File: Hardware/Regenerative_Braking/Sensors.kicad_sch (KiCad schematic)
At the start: 0 parts

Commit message: edited till inverter circuit
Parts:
- added ACS712-30A1, ACS712-30A2, ACS712-30A3: (no value), Regen_braking:ACS712_Module_27x12mm, symbol Regen_braking:ACS712-30A
- added ACS712-30A4, ACS712-30A5, ACS712-30A6: (no value), Regen_braking:Solderpad_acs712_INOUT, symbol Regen_braking:solder_pad_acs712_inout
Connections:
- new net 5V: ACS712-30A1. (VCC), ACS712-30A2. (VCC), ACS712-30A3. (VCC)
- new net GND: ACS712-30A1. (VCC), ACS712-30A2. (VCC), ACS712-30A3. (VCC), ACS712-30A4. (OUT), ACS712-30A5. (OUT), ACS712-30A6. (OUT)
- new net Iin1: ACS712-30A4. (OUT)
- new net Iin2: ACS712-30A5. (OUT)
- new net Iin3: ACS712-30A6. (OUT)
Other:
- note added: "INVERTER SIDE CURRENT SENSING"

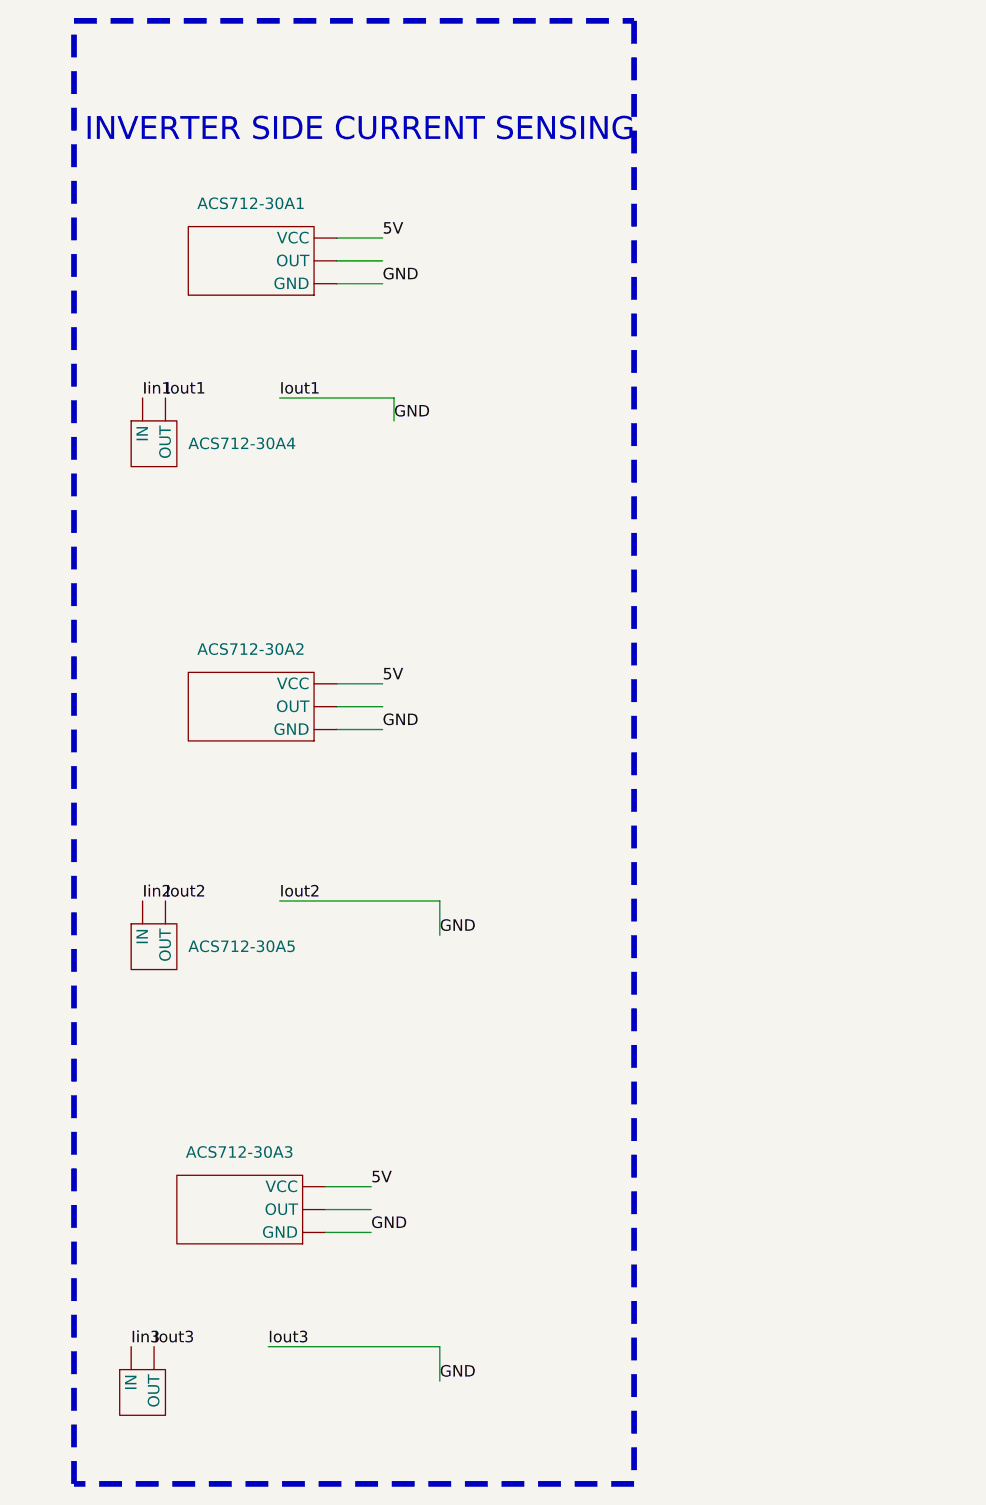
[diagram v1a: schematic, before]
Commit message: started with sensing circuits
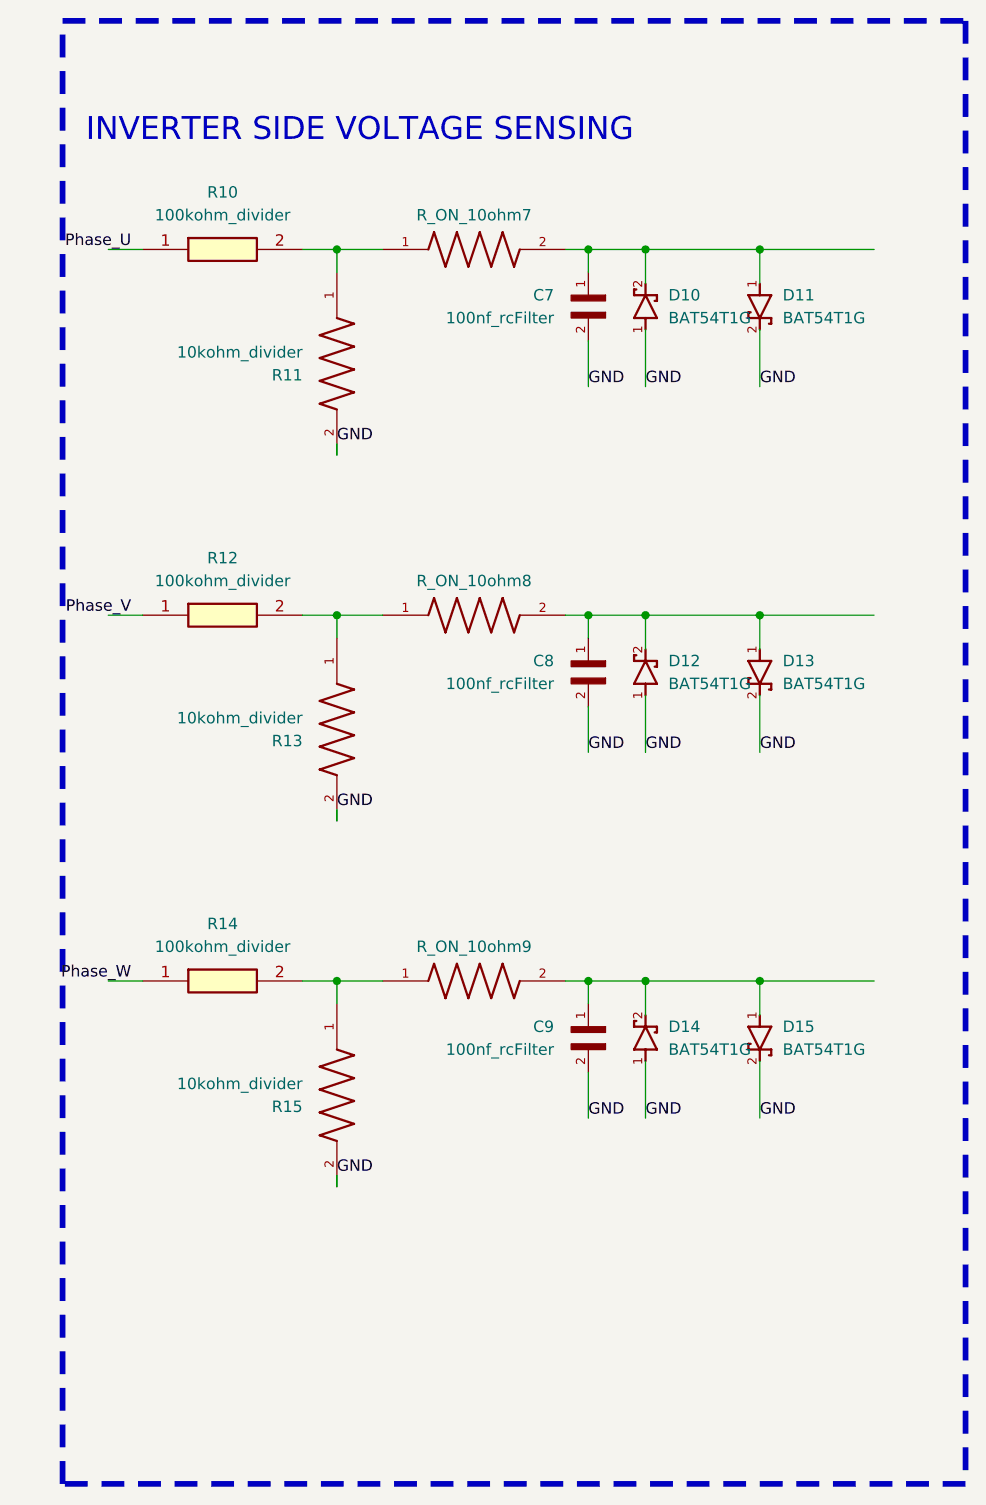
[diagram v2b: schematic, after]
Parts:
- removed ACS712-30A1, ACS712-30A2, ACS712-30A3: (no value), Regen_braking:ACS712_Module_27x12mm, symbol Regen_braking:ACS712-30A
- removed ACS712-30A4, ACS712-30A5, ACS712-30A6: (no value), Regen_braking:Solderpad_acs712_INOUT, symbol Regen_braking:solder_pad_acs712_inout
- added C7, C8, C9: 100nf_rcFilter, Regen_braking:100nf_rcFilter, symbol Regen_braking:100nf_rcFilter
- added D10, D11, D12, D13, D14, D15: BAT54T1G, Regen_braking:BAT54T1G, symbol Regen_braking:BAT54T1G
- added R10, R12, R14: 100kohm_divider, Regen_braking:100kohm_divider, symbol Regen_braking:100kohm_divider
- added R11, R13, R15: 10kohm_divider, Regen_braking:10kohm_divider, symbol Regen_braking:10kohm_divider
- added R_ON_10ohm7, R_ON_10ohm8, R_ON_10ohm9: (no value), Regen_braking:R_ON_10ohm, symbol Regen_braking:R_ON_10ohm
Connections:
- net GND: now also C7.2, C8.2, C9.2, D10.1, D11.2, D12.1, D13.2, D14.1, D15.2, R11.2, R13.2, R15.2
- new net: C7.1, D10.2, D11.1, R_ON_10ohm7.2
- new net: C9.1, D14.2, D15.1, R_ON_10ohm9.2
- new net: R14.2, R15.1, R_ON_10ohm9.1
- new net: R12.2, R13.1, R_ON_10ohm8.1
- new net: C8.1, D12.2, D13.1, R_ON_10ohm8.2
- new net: R10.2, R11.1, R_ON_10ohm7.1
- new net Phase_U: R10.1
- new net Phase_V: R12.1
- new net Phase_W: R14.1
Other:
- note added: "INVERTER SIDE VOLTAGE SENSING"
- note removed: "INVERTER SIDE CURRENT SENSING"

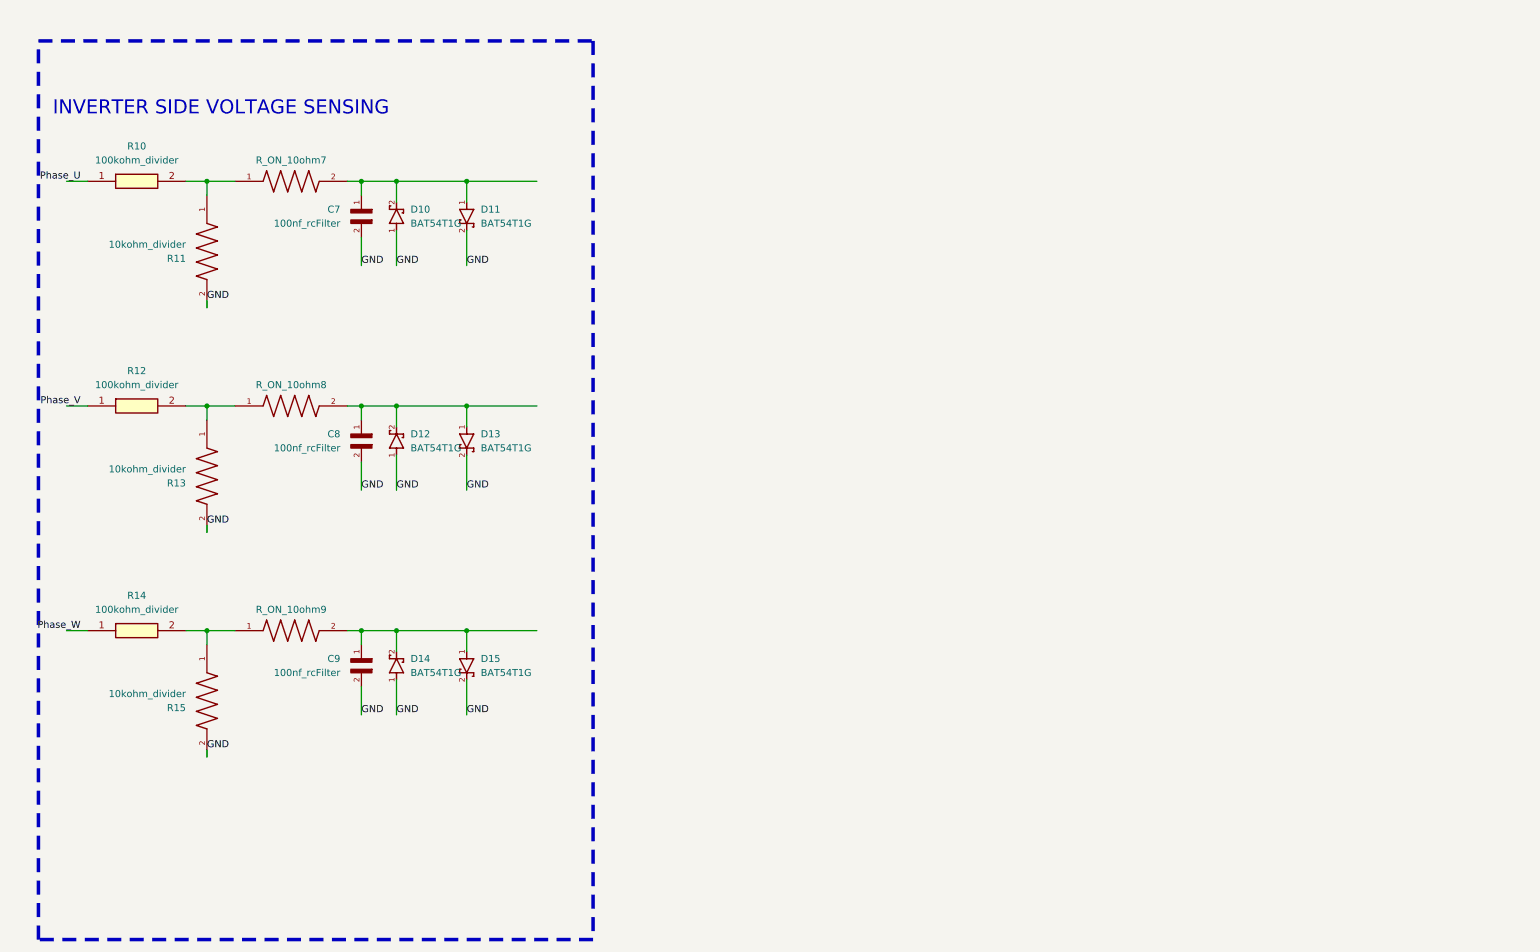
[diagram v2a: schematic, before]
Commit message: finished with sensing circuits & cap banks
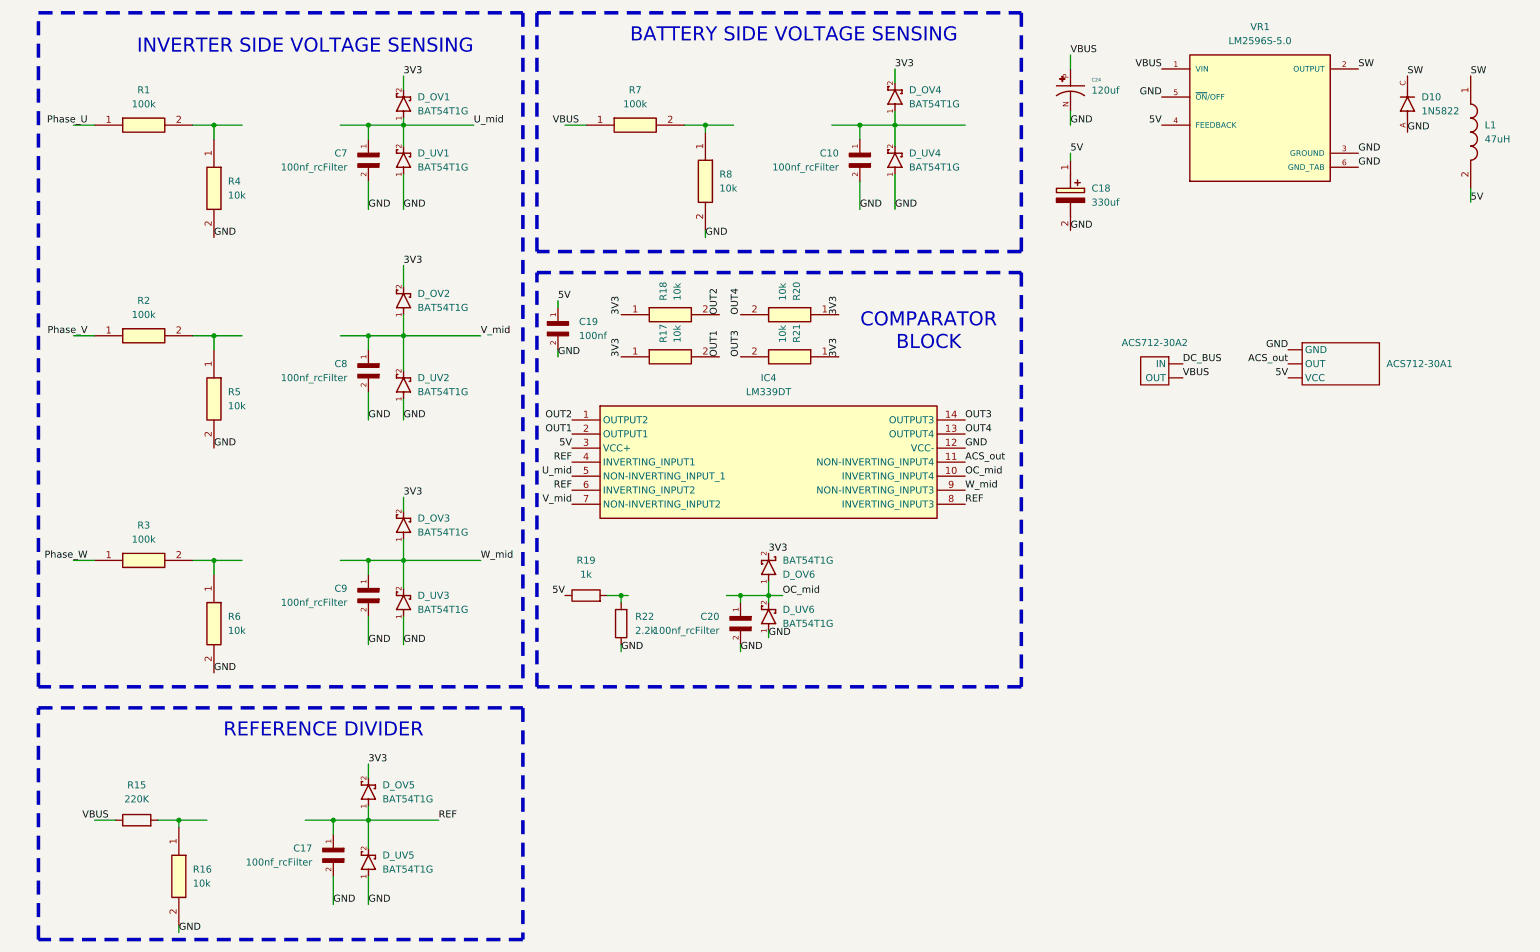
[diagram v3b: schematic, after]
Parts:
- removed D11, D12, D13, D14, D15: BAT54T1G, Regen_braking:BAT54T1G, symbol Regen_braking:BAT54T1G
- removed R10, R12, R14: 100kohm_divider, Regen_braking:100kohm_divider, symbol Regen_braking:100kohm_divider
- removed R11, R13, R15: 10kohm_divider, Regen_braking:10kohm_divider, symbol Regen_braking:10kohm_divider
- removed R_ON_10ohm7, R_ON_10ohm8, R_ON_10ohm9: (no value), Regen_braking:R_ON_10ohm, symbol Regen_braking:R_ON_10ohm
- added ACS712-30A1: (no value), Regen_braking:ACS712_Module_27x12mm, symbol Regen_braking:ACS712-30A
- added ACS712-30A2: (no value), Regen_braking:Solderpad_acs712_INOUT, symbol Regen_braking:solder_pad_acs712_inout
- added C10, C17, C20: 100nf_rcFilter, Regen_braking:100nf_rcFilter, symbol Regen_braking:100nf_rcFilter
- added C18: 330uf, Regen_braking:330uf_25v_cap_5v_buck, symbol Regen_braking:330uf_25v_cap_5v_buck
- added C19: 100nf, C1206C104J5RACTU:CAPC3216X88N, symbol Regen_braking:100nf_rcFilter
- added C24: 120uf, Regen_braking:120uf_cap_5v_buck, symbol Regen_braking:120uf_cap_5v_buck
- added D10: 1N5822, Regen_braking:1N5822, symbol Regen_braking:1N5822
- added D_OV2, D_OV3, D_OV4, D_OV5, D_OV6, D_UV1, D_UV2, D_UV3, D_UV4, D_UV5, D_UV6: BAT54T1G, Regen_braking:BAT54T1G, symbol Regen_braking:BAT54T1G
- added IC4: LM339DT, Regen_braking:LM339DT, symbol Regen_braking:LM339DT
- added L1: 47uH, Regen_braking:47uh_5v_buck, symbol Regen_braking:47uh_5v_buck
- added R1, R2, R3, R7: 100k, Regen_braking:47,2.2,100k,10k,4.7,10ohm, symbol Regen_braking:47,2.2,100k,10k,4.7,10ohm
- added R15: 220K, Regen_braking:220kohm_divider, symbol Device:R
- added R16, R17, R18, R20, R21, R4, R5, R6, R8: 10k, Regen_braking:47,2.2,100k,10k,4.7,10ohm, symbol Regen_braking:47,2.2,100k,10k,4.7,10ohm
- added R19: 1k, Regen_braking:47,2.2,100k,10k,4.7,10ohm, symbol Device:R
- added R22: 2.2k, Regen_braking:47,2.2,100k,10k,4.7,10ohm, symbol Device:R
- added VR1: LM2596S-5.0, Regen_braking:5v_buck, symbol Regen_braking:LM2596S-5.0
- renumbered D10 to D_OV1
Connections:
- net GND: now also ACS712-30A1. (VCC), C10.2, C17.2, C18.2 (-), C19.2, C20.2, C24.N, D10.A, D_UV1.1, D_UV2.1, D_UV3.1, D_UV4.1, D_UV5.1, D_UV6.1, IC4.12 (VCC-), R16.2, R22.1, R4.2, R5.2, R6.2, R8.2, VR1.3 (GROUND), VR1.5 (~{ON}/OFF), VR1.6 (GND_TAB); no longer D_OV1.1
- net Phase_U: now also R1.1
- net Phase_V: now also R2.1
- net Phase_W: now also R3.1
- net 3V3: now reaches D_OV1.2
- net 3V3: now also D_OV2.2, D_OV3.2, D_OV4.2, D_OV5.2, D_OV6.2, R17.1, R18.1, R20.1, R21.1; no longer C7.1
- net W_mid: now reaches C9.1
- net W_mid: now also D_OV3.1, D_UV3.2, IC4.9 (NON-INVERTING_INPUT3)
- net V_mid: now reaches C8.1
- net V_mid: now also D_OV2.1, D_UV2.2, IC4.7 (NON-INVERTING_INPUT2)
- new net: R15.2, R16.1
- new net: R7.2, R8.1
- new net: C10.1, D_OV4.1, D_UV4.2
- new net: R1.2, R4.1
- new net: R19.2, R22.2
- new net: R2.2, R5.1
- new net: R3.2, R6.1
- new net 5V: ACS712-30A1. (VCC), C18.1 (+), C19.1, IC4.3 (VCC+), L1.2, R19.1, VR1.4 (FEEDBACK)
- new net ACS_out: ACS712-30A1. (VCC), IC4.11 (NON-INVERTING_INPUT4)
- new net DC_BUS: ACS712-30A2. (OUT)
- new net OC_mid: C20.1, D_OV6.1, D_UV6.2, IC4.10 (INVERTING_INPUT4)
- new net OUT1: IC4.2 (OUTPUT1), R17.2
- new net OUT2: IC4.1 (OUTPUT2), R18.2
- new net OUT3: IC4.14 (OUTPUT3), R21.2
- new net OUT4: IC4.13 (OUTPUT4), R20.2
- new net REF: C17.1, D_OV5.1, D_UV5.2, IC4.4 (INVERTING_INPUT1), IC4.6 (INVERTING_INPUT2), IC4.8 (INVERTING_INPUT3)
- new net SW: D10.C, L1.1, VR1.2 (OUTPUT)
- new net U_mid: C7.1, D_OV1.1, D_UV1.2, IC4.5 (NON-INVERTING_INPUT_1)
- new net VBUS: ACS712-30A2. (OUT), C24.P, R15.1, R7.1, VR1.1 (VIN)
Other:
- note added: "BATTERY SIDE VOLTAGE SENSING"
- note added: "COMPARATOR BLOCK"
- note added: "REFERENCE DIVIDER"
- moved on the sheet: C7, C8, C9, D_OV1

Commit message: finished with sensing circuits & cap banks
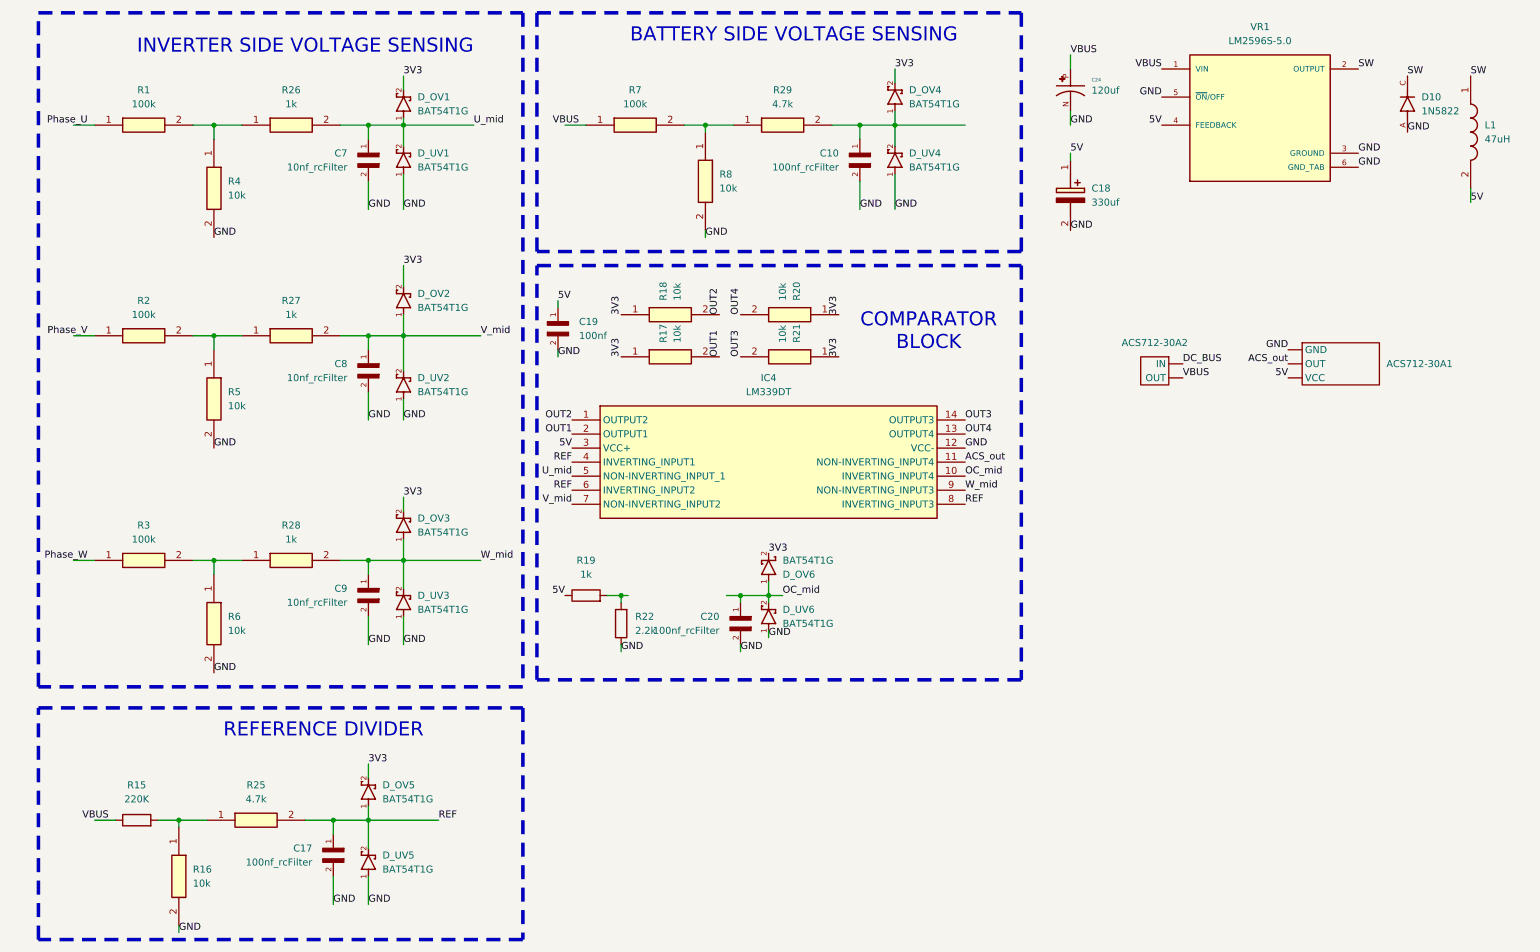
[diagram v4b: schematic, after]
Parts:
- added R25, R29: 4.7k, Regen_braking:47,2.2,100k,10k,4.7,10ohm, symbol Regen_braking:47,2.2,100k,10k,4.7,10ohm
- added R26, R27, R28: 1k, Regen_braking:47,2.2,100k,10k,4.7,10ohm, symbol Regen_braking:47,2.2,100k,10k,4.7,10ohm
- C7, C8, C9: value 100nf_rcFilter -> 10nf_rcFilter
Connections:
- net REF: now also R25.2
- net U_mid: now also R26.2
- net V_mid: now also R27.2
- net W_mid: now also R28.2
- net at R15.2, R16.1: now also R25.1
- net at R7.2, R8.1: now also R29.1
- net at C10.1, D_OV4.1, D_UV4.2: now also R29.2
- net at R1.2, R4.1: now also R26.1
- net at R2.2, R5.1: now also R27.1
- net at R3.2, R6.1: now also R28.1
